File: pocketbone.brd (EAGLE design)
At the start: 55 x 35 mm, 60 parts, among them J1 USD_CONNECTOR, U1 24LC_32AT-I/OT, U2 OSD3358, U3 SN74LVC1G07_DCK_5, Y1 CM200C-32.768KAZF-UT, Y2 445C33D24M00000

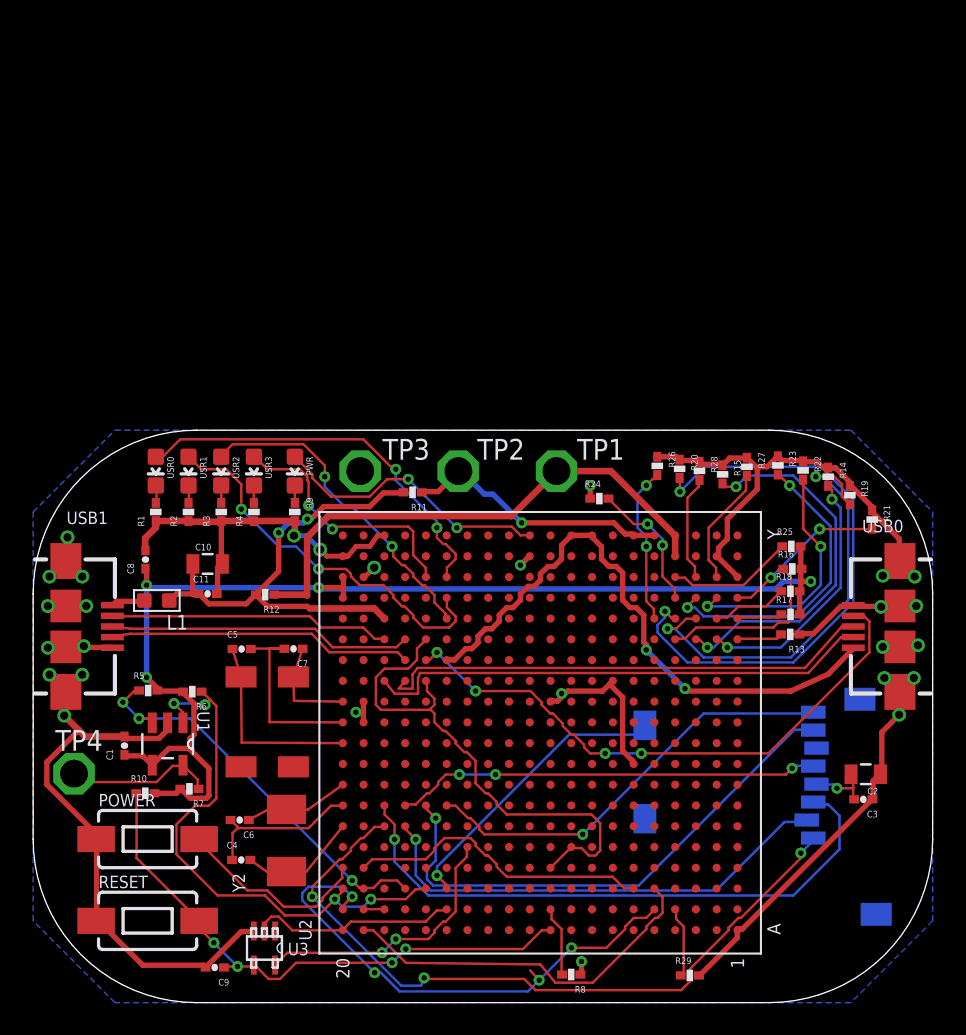
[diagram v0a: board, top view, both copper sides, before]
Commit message: Reduce size (WIP) and change DRU for Seeed Studio tolerances
Signed-off-by: Andrew Yong <me@ndoo.sg>
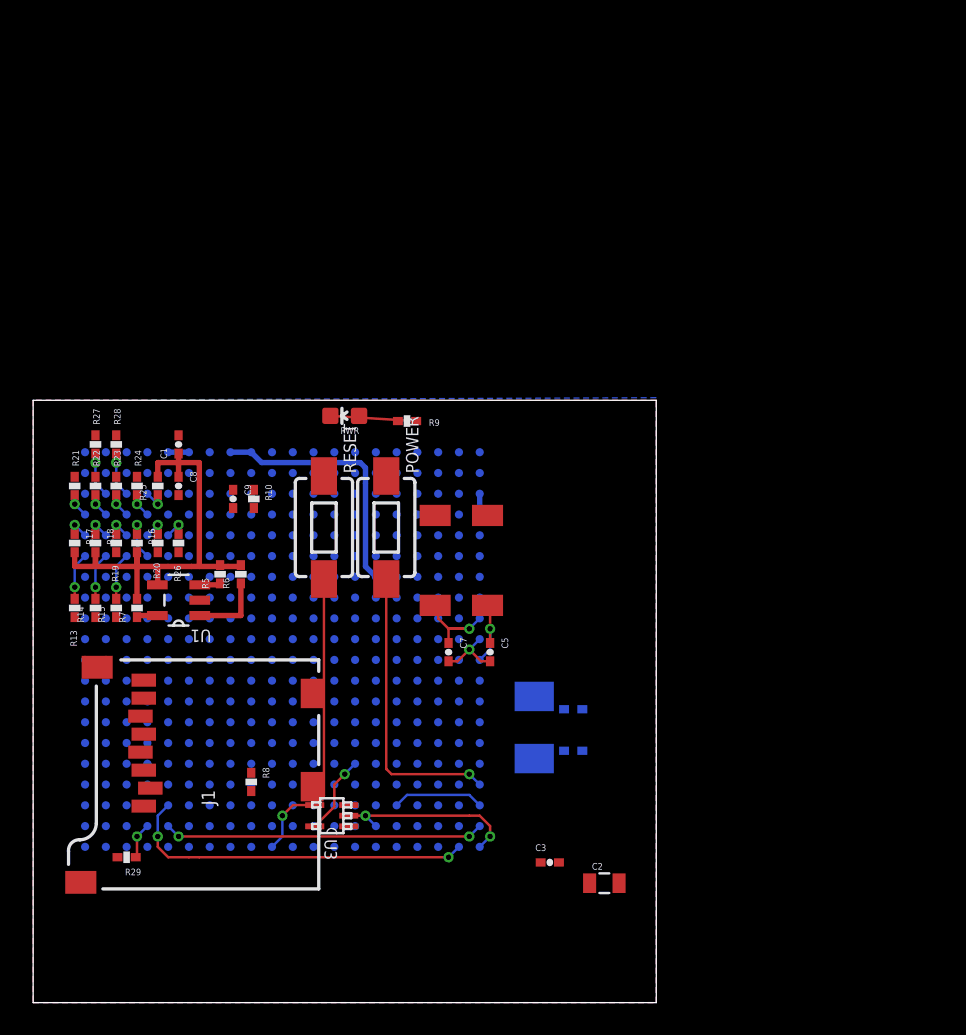
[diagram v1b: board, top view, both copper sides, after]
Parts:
- removed C10: 10uF, Strawson_Eagle_Lib:0805
- removed C11: 0.1uF, Strawson_Eagle_Lib:0402-CAP
- removed L1: 120, Seeed-OPL-Inductor:L0603
- removed R1, R2, R3, R4: 240, Strawson_Eagle_Lib:0402-RES
- removed R11: 0, Strawson_Eagle_Lib:0402-RES
- removed R12: 0,DNI, Strawson_Eagle_Lib:0402-RES
- removed TP1, TP2, TP3, TP4: TPSQPAD1-17, pocketbone:P1-17
- removed USB0, USB1: USB-MICRO-SMD, pocketbone:USB-AB-MICRO-SMD
- removed USR0, USR1, USR2, USR3: BLUE, BeagleBone_Blue:LED-0603
- moved R21 48.8 mm to (2.54, 31.6)
- moved R14 45.5 mm to (3.81, 24.1), turned to 90 degrees
- moved R19 45.0 mm to (5.08, 28.1), turned to 90 degrees
- moved R17 44.0 mm to (2.54, 28.1), turned to 270 degrees
- moved R13 43.8 mm to (2.54, 24.1), turned to 90 degrees
- moved R22 43.3 mm to (3.81, 31.6)
- moved R18 42.6 mm to (3.81, 28.1), turned to 270 degrees
- moved R23 40.5 mm to (5.08, 31.6)
- moved R16 40.1 mm to (6.35, 28.1), turned to 270 degrees
- moved R27 39.9 mm to (3.81, 34.1)
- moved R25 38.9 mm to (7.62, 31.6), turned to 90 degrees
- moved R15 38.0 mm to (5.08, 24.1), turned to 90 degrees
- moved R28 35.7 mm to (5.08, 34.1)
- moved R29 35.2 mm to (5.71, 8.89), turned to 180 degrees
- moved R20 32.2 mm to (7.62, 28.1), turned to 90 degrees
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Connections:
- removed net N$1: L1.2, USB1.VBUS
- removed net N$129: C10.1, C11.1, L1.1, R11.2, R12.2, U2.T18
- removed net N$43: U2.V16, USR3.A
- removed net N$44: U2.T15, USR2.A
- removed net N$45: U2.U15, USR1.A
- removed net N$46: U2.V15, USR0.A
- removed net N$47: R1.2, USR0.C
- removed net N$57: R2.2, USR1.C
- removed net N$58: R3.2, USR2.C
- removed net N$59: R4.2, USR3.C
- removed net SYS_5V: R12.1, TP1.TP, U2.W4, U2.Y4
- removed net USB1_DM: U2.R18, USB1.D-
- removed net USB1_DP: U2.R17, USB1.D+
- removed net USB1_ID: U2.P17, USB1.ID
- removed net VDD_1V8: U2.D10, U2.E9, U2.N16, U2.R16
- new net VCC_3V3B: C2.2, C3.2, J1.VCC
- new net VOUT_LDO3_1P8V_0: U2.N16
- new net VOUT_LDO3_1P8V_1: U2.R16
- new net VOUT_SYS_5V_0: U2.W4
- new net VOUT_SYS_5V_1: U2.Y4
- net 3.3V: no longer C2.2, C3.2, J1.VCC
- net 5.0V: no longer R11.1, TP2.TP
- net GND: now also R9.1; no longer C10.2, C11.2, R1.1, R2.1, R3.1, R4.1, R9.2, TP3.TP, USB0.GND, USB0.SHIELD1, USB0.SHIELD2, USB0.SHIELD3, USB0.SHIELD4, USB1.GND, USB1.SHIELD1, USB1.SHIELD2, USB1.SHIELD3, USB1.SHIELD4
- net N$28: no longer TP4.TP
- net PWR_LEDR: now also R9.2; no longer R9.1
- net USB0_DM: no longer USB0.D-
- net USB0_DP: no longer USB0.D+
- net USB0_ID: no longer USB0.ID
- net USB_DC: no longer USB0.VBUS
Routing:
- net GND: track 137.6 -> 0.00 mm, vias 27 -> 0
- net 3.3V: track 77.6 -> 30.3 mm, vias 5 -> 0
- net NTE: track 44.9 -> 0.00 mm, vias 3 -> 0
- net N$74: track 37.0 -> 0.00 mm, vias 1 -> 0
- net USB0_ID: track 35.7 -> 0.00 mm, vias 4 -> 0
- net SVO6: track 35.8 -> 1.45 mm, vias 2 -> 1
- net N$77: track 32.7 -> 0.00 mm, vias 1 -> 0
- net SYS_5V: track 32.7 -> 0.00 mm
- net VDD_1V8: track 31.8 -> 0.00 mm
- net USB0_DM: track 31.2 -> 0.00 mm
- net USB0_DP: track 30.7 -> 0.00 mm
- net N$5: track 29.3 -> 0.00 mm, vias 1 -> 0
- net N$129: track 29.3 -> 0.00 mm, vias 2 -> 0
- net N$70: track 26.3 -> 0.00 mm, vias 1 -> 0
- net N$2: track 26.1 -> 0.00 mm, vias 3 -> 0
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- added copper zone on layer 1, net GND
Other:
- board size 55 x 35 mm -> 38.1 x 36.8 mm

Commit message: Route XTAL
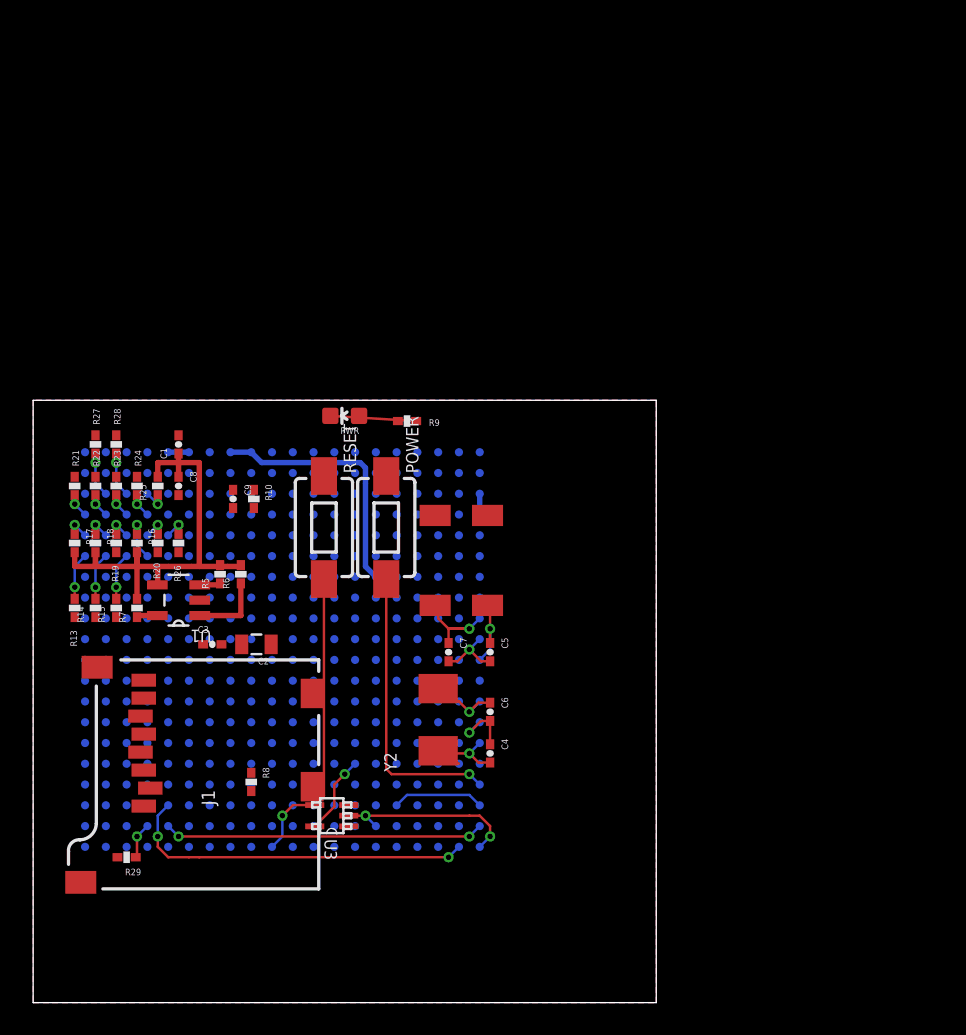
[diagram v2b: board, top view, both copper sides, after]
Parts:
- moved C2 25.8 mm to (13.7, 21.9), turned to 180 degrees
- moved C3 24.6 mm to (11.0, 21.9)
- moved C4 5.08 mm to (27.9, 15.2), flipped to the top, turned to 270 degrees
- moved C6 5.08 mm to (27.9, 17.8), flipped to the top, turned to 270 degrees
- moved Y2 0.93 mm to (27.3, 14.1), flipped to the top
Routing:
- net N$33: track 0.00 -> 5.49 mm, vias 0 -> 1
- net N$32: track 0.00 -> 4.79 mm, vias 0 -> 1
- net N$34: track 0.00 -> 3.89 mm, vias 0 -> 1
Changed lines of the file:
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@@
 <element name="C5" library="Strawson_Eagle_Lib" package="0402-CAP" value="20pF" x="27.94" y="21.43125" rot="R270"/>
 <element name="C7" library="Strawson_Eagle_Lib" package="0402-CAP" value="20pF" x="25.4" y="21.43125" rot="R270"/>
-<element name="C6" library="Strawson_Eagle_Lib" package="0402-CAP" value="20pF" x="33.02" y="17.93875" rot="MR180"/>
-<element name="C4" library="Strawson_Eagle_Lib" package="0402-CAP" value="20pF" x="33.02" y="15.39875" rot="MR0"/>
+<element name="C6" library="Strawson_Eagle_Lib" package="0402-CAP" value="20pF" x="27.94" y="17.78" rot="R270"/>
+<element name="C4" library="Strawson_Eagle_Lib" package="0402-CAP" value="20pF" x="27.94" y="15.24" rot="R270"/>
 <element name="C9" library="Strawson_Eagle_Lib" package="0402-CAP" value="1uF" x="12.22375" y="30.7975" rot="R270"/>
-<element name="C2" library="Strawson_Eagle_Lib" package="0805" value="10uF" x="34.925" y="7.3025"/>
-<element name="C3" library="Strawson_Eagle_Lib" package="0402-CAP" value="0.1uF" x="31.59125" y="8.5725"/>
+<element name="C2" library="Strawson_Eagle_Lib" package="0805" value="10uF" x="13.6525" y="21.9075" rot="R180"/>
+<element name="C3" library="Strawson_Eagle_Lib" package="0402-CAP" value="0.1uF" x="10.95375" y="21.9075"/>
 <element name="PWR" library="BeagleBone_Blue" package="LED-0603" value="BLUE" x="19.05" y="35.8775" rot="R90"/>
 <element name="J1" library="pocketbone" package="MICRO-SD-SOCKET-PP" value="USD_CONNECTOR" x="17.4625" y="20.955" rot="R90">
@@
 </element>
 <element name="Y1" library="pocketbone" package="CM200C-32.768KAZF-UT" value="CM200C-32.768KAZF-UT" x="30.32125" y="23.01875" rot="R90"/>
-<element name="Y2" library="pocketbone" package="445C33D24M00000" value="445C33D24M00000" x="28.09875" y="13.6525" rot="MR90"/>
+<element name="Y2" library="pocketbone" package="445C33D24M00000" value="445C33D24M00000" x="27.305" y="14.12875" rot="R90"/>
 <element name="POWER" library="SparkFun-Electromechanical" package="TACTILE-SWITCH-1101NE" value="SWITCH-MOMENTARY-2SMD-1101NE" x="21.59" y="29.05125" smashed="yes" rot="R270">
 <attribute name="PROD_ID" value="SWCH-00815" x="21.59" y="29.05125" size="1.778" layer="27" rot="R270" display="off"/>
@@
 </polygon>
 <polygon width="0.3302" layer="16">
-<vertex x="38.1" y="36.98875"/>
+<vertex x="38.1" y="36.83"/>
 <vertex x="0" y="36.83"/>
 <vertex x="0" y="0"/>
@@
 <contactref element="C6" pad="1"/>
 <contactref element="Y2" pad="2"/>
-<wire x1="30.63875" y1="18.7225" x2="32.4612" y2="17.93875" width="0" layer="19" extent="16-16"/>
-<wire x1="27.305" y1="18.415" x2="30.63875" y2="18.7225" width="0" layer="19" extent="16-16"/>
+<wire x1="27.305" y1="18.415" x2="26.67" y2="17.78" width="0.1524" layer="16"/>
+<via x="26.67" y="17.78" extent="1-16" drill="0.3302" shape="octagon"/>
+<wire x1="26.67" y1="17.78" x2="27.2288" y2="18.3388" width="0.1524" layer="1"/>
+<wire x1="27.2288" y1="18.3388" x2="27.94" y2="18.3388" width="0.1524" layer="1"/>
+<wire x1="26.67" y1="17.78" x2="26.045" y2="18.405" width="0.1524" layer="1"/>
+<wire x1="26.045" y1="18.405" x2="24.765" y2="19.19875" width="0.1524" layer="1"/>
 </signal>
 <signal name="N$33">
@@
 <contactref element="C4" pad="2"/>
 <contactref element="Y2" pad="1"/>
-<wire x1="30.63875" y1="14.9225" x2="32.4612" y2="15.39875" width="0" layer="19" extent="16-16"/>
-<wire x1="27.305" y1="15.875" x2="30.63875" y2="14.9225" width="0" layer="19" extent="16-16"/>
+<wire x1="27.305" y1="15.875" x2="26.67" y2="15.24" width="0.1524" layer="16"/>
+<via x="26.67" y="15.24" extent="1-16" drill="0.3302" shape="octagon"/>
+<wire x1="26.67" y1="15.24" x2="27.2288" y2="14.6812" width="0.1524" layer="1"/>
+<wire x1="27.2288" y1="14.6812" x2="27.94" y2="14.6812" width="0.1524" layer="1"/>
+<wire x1="26.035" y1="14.605" x2="25.17881875" y2="15.1401125" width="0.1524" layer="1"/>
+<wire x1="25.17881875" y1="15.1401125" x2="24.765" y2="15.39875" width="0.1524" layer="1"/>
+<wire x1="26.67" y1="15.24" x2="25.17881875" y2="15.24" width="0.1524" layer="1"/>
+<wire x1="25.17881875" y1="15.24" x2="25.17881875" y2="15.1401125" width="0.1524" layer="1"/>
 </signal>
 <signal name="N$34">
@@
 <contactref element="U2" pad="G20"/>
 <contactref element="C6" pad="2"/>
-<wire x1="33.5788" y1="15.39875" x2="33.5788" y2="17.93875" width="0" layer="19" extent="16-16"/>
-<wire x1="27.305" y1="17.145" x2="33.5788" y2="17.93875" width="0" layer="19" extent="16-16"/>
+<wire x1="27.305" y1="17.145" x2="26.67" y2="16.51" width="0.1524" layer="16"/>
+<via x="26.67" y="16.51" extent="1-16" drill="0.3302" shape="octagon"/>
+<wire x1="26.67" y1="16.51" x2="27.3812" y2="17.2212" width="0.1524" layer="1"/>
+<wire x1="27.3812" y1="17.2212" x2="27.94" y2="17.2212" width="0.1524" layer="1"/>
+<wire x1="27.94" y1="17.2212" x2="27.94" y2="15.7988" width="0.1524" layer="1"/>
 </signal>
 <signal name="N$42">
@@
 <contactref element="C2" pad="2"/>
 <contactref element="J1" pad="VCC"/>
-<wire x1="32.15005" y1="8.5725" x2="35.825" y2="7.3025" width="0" layer="19" extent="1-1"/>
-<wire x1="6.5625" y1="15.315" x2="32.15005" y2="8.5725" width="0" layer="19" extent="1-1"/>
+<wire x1="11.51255" y1="21.9075" x2="12.7525" y2="21.9075" width="0" layer="19" extent="1-1"/>
+<wire x1="6.5625" y1="15.315" x2="11.51255" y2="21.9075" width="0" layer="19" extent="1-1"/>
 </signal>
 <signal name="NTE">

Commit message: Add the missing 2xµUSB OTG ports, cleanup
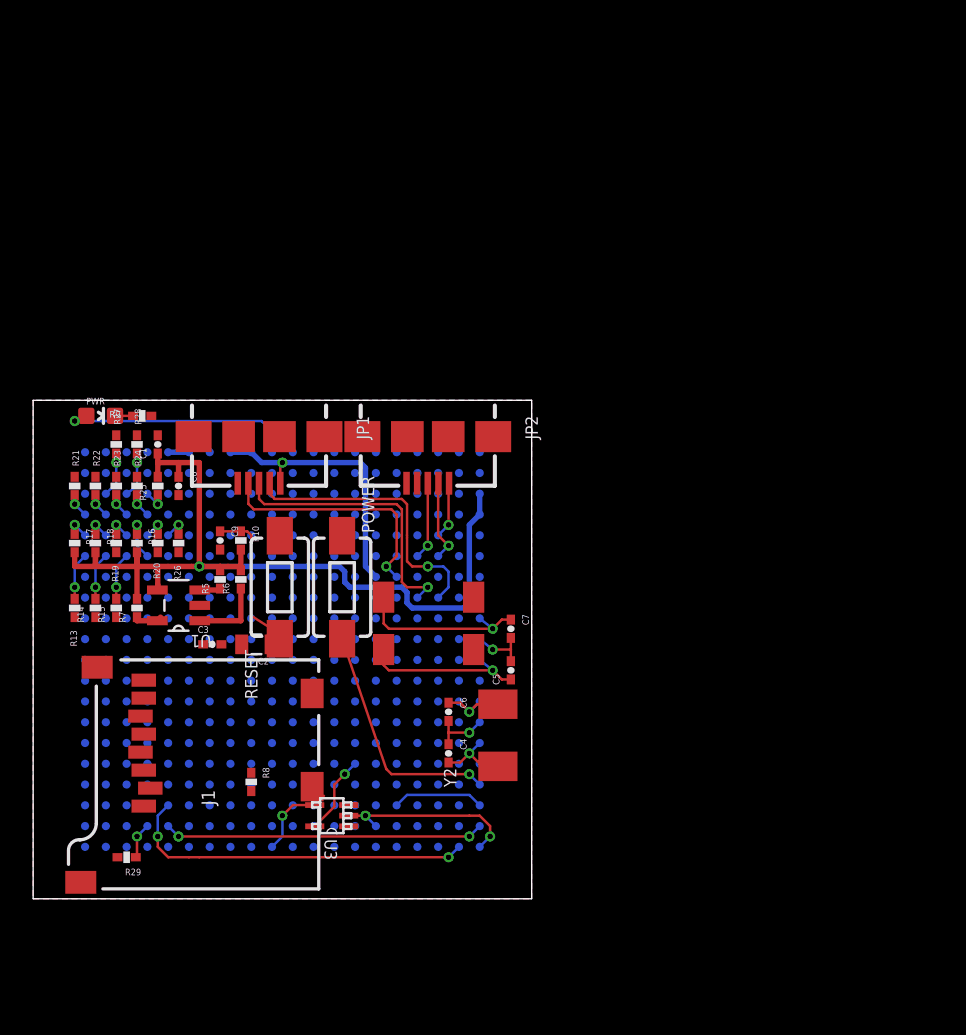
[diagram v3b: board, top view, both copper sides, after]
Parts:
- added JP1, JP2: (no value), pocketbone:USB-AB-MICRO-SMD
- moved R9 16.2 mm to (6.67, 35.9), turned to 180 degrees
- moved PWR 14.9 mm to (4.13, 35.9), turned to 270 degrees
- moved Y1 10.9 mm to (20.2, 19.1), turned to 0 degrees
- moved POWER 4.54 mm to (18.9, 25.4)
- moved RESET 4.54 mm to (15.1, 25.4)
- moved C7 4.07 mm to (29.2, 22.9)
- moved Y2 3.77 mm to (31.0, 13.2)
- moved C9 2.66 mm to (11.4, 28.3)
- moved R10 2.66 mm to (12.7, 28.3)
- moved C4 2.54 mm to (25.4, 15.2)
- moved C6 2.54 mm to (25.4, 17.8)
- moved C5 1.69 mm to (29.2, 20.3), turned to 90 degrees
- moved C1 1.27 mm to (7.62, 34.1)
- moved R27 1.27 mm to (5.08, 34.1)
- moved R28 1.27 mm to (6.35, 34.1)
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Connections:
- new net N$1: JP2.D+, U2.R17
- new net N$4: JP2.D-, U2.R18
- new net N$6: JP2.VBUS, U2.T18
- net GND: now also JP1.GND, JP1.SHIELD1, JP1.SHIELD2, JP1.SHIELD3, JP1.SHIELD4, JP2.GND, JP2.SHIELD1, JP2.SHIELD2, JP2.SHIELD3, JP2.SHIELD4
- net USB0_DM: now also JP1.D-
- net USB0_DP: now also JP1.D+
- net USB0_ID: now also JP1.ID
- net USB_DC: now also JP1.VBUS
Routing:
- net 3.3V: track 30.3 -> 56.5 mm, vias 0 -> 1
- net USB0_DM: track 0.00 -> 17.5 mm, vias 0 -> 1
- net USB0_DP: track 0.00 -> 17.0 mm, vias 0 -> 1
- net VDD_3V3AUX: track 0.00 -> 15.0 mm, vias 0 -> 1
- net USB0_ID: track 0.00 -> 14.9 mm, vias 0 -> 1
- net N$27: track 4.63 -> 10.1 mm
- net N$4: track 0.00 -> 4.99 mm, vias 0 -> 1
- net N$1: track 0.00 -> 4.72 mm, vias 0 -> 1
- net N$26: track 6.08 -> 10.8 mm
- net RESET: track 18.8 -> 14.6 mm
- net PWR_LEDR: track 5.26 -> 1.10 mm
- net N$6: track 0.00 -> 3.46 mm, vias 0 -> 1
- net PWR: track 17.7 -> 14.5 mm
- net USB_DC: track 15.6 -> 17.1 mm, vias 0 -> 1
- net N$33: track 5.49 -> 4.47 mm
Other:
- board size 38.1 x 36.8 mm -> 30.5 x 30.5 mm

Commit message: Added AR8035 PHY (layout not done), reduced size
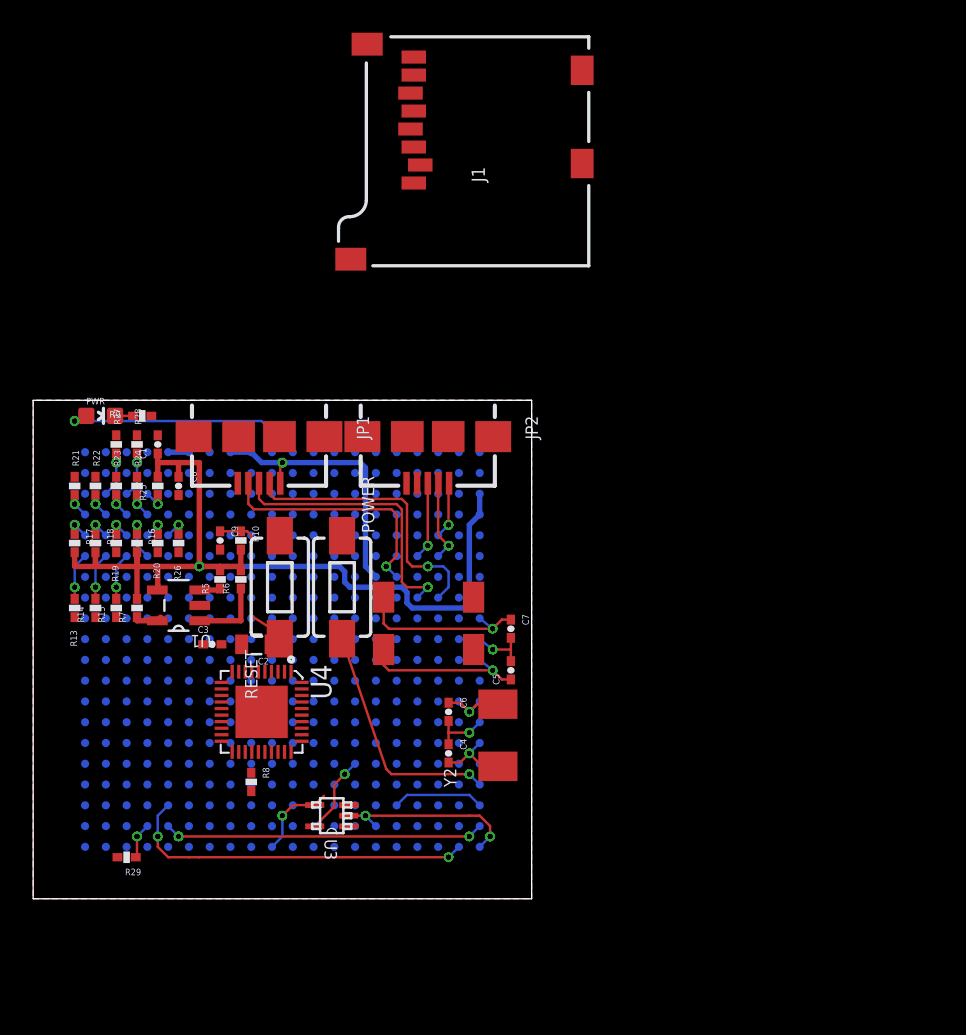
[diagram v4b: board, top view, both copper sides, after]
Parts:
- added U4: AR8035-AL1B, AR8035-AL1B:QFN40P500X500X75-41N
- moved J1 41.5 mm to (34.0, 59.1)
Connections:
- new net AVDD33: U4.14
- new net AVDDL: U4.11, U4.17, U4.6
- new net DVDDL: U4.38
- new net MDC: U2.M18, U4.40
- new net MDIO: U2.M17
- new net MII1_COL: U2.H16
- new net MII1_CRS: U2.H17
- new net MII1_REF_CLK: U2.H18
- new net MII1_RXD0: U2.M16, U4.29
- new net MII1_RXD1: U2.L15, U4.28
- new net MII1_RXD2: U2.L16, U4.26
- new net MII1_RXD3: U2.L17, U4.25
- new net MII1_RX_CLK: U2.L18, U4.31
- new net MII1_RX_DV: U2.J17, U4.30
- new net MII1_RX_ER: U2.J15
- new net MII1_TXD0: U2.K17, U4.34
- new net MII1_TXD1: U2.K16, U4.35
- new net MII1_TXD2: U2.K15, U4.36
- new net MII1_TXD3: U2.J18, U4.37
- new net MII1_TX_CLK: U2.K18
- new net MII1_TX_EN: U2.J16, U4.32
- new net N$14: U4.9
- new net N$15: U4.12
- new net N$16: U4.15
- new net N$17: U4.18
- new net N$18: U4.33
- new net N$19: U4.10
- new net N$20: U4.13
- new net N$21: U4.16
- new net N$22: U4.19
- new net N$23: U4.27
- new net N$24: U4.8
- new net N$7: U4.41
- new net VDD33: U4.3
